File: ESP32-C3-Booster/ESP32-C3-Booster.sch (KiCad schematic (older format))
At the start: 0 parts

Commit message: Almost done with ESP32-C3-Booster.
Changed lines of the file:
@@
 F0 "ESP32-C3 MCU" 60
 F1 "ESP32-C3-MCU.sch" 60
+F2 "GPIO0/A1/CurrentSense" I L 5100 3150 60
+F3 "GPIO1/A2/TermpSense" I R 7250 2250 60
+F4 "GPIO2/Fan" O R 7250 2000 60
+F5 "CAN_TX" O L 5100 1700 60
+F6 "CAN_RX" I L 5100 1900 60
 $EndSheet
 $Sheet
@@
 F4 "BRAKE" I L 5000 4350 60
 F5 "PowerIn" I L 5000 4500 60
-F6 "A" O L 5000 4650 60
-F7 "B" O L 5000 4800 60
+F6 "A" O R 7150 4550 60
+F7 "B" O R 7150 4800 60
 F8 "Sense_Pos" O L 5000 5050 60
 F9 "Sense_Neg" O L 5000 5200 60
@@
 F2 "FAN_POWER" I L 7950 1800 60
 F3 "FAN_CONTROL" I L 7950 2000 60
-F4 "TEMP_SENSE" O L 7950 2200 60
+F4 "TEMP_SENSE" O L 7950 2250 60
 $EndSheet
+Wire Wire Line
+	3500 1700 5100 1700
+Wire Wire Line
+	3500 1900 5100 1900
+$Comp
+L +3.3V #PWR?
+U 1 1 630B61AD
+P 3750 4100
+F 0 "#PWR?" H 3750 3950 50  0001 C CNN
+F 1 "+3.3V" H 3750 4240 50  0000 C CNN
+F 2 "" H 3750 4100 50  0001 C CNN
+F 3 "" H 3750 4100 50  0001 C CNN
+	1    3750 4100
+	1    0    0    -1
+$EndComp
+Wire Wire Line
+	3750 4100 3750 4150
+Wire Wire Line
+	3750 4150 3500 4150
+$Comp
+L +12V #PWR?
+U 1 1 630B6295
+P 3800 4600
+F 0 "#PWR?" H 3800 4450 50  0001 C CNN
+F 1 "+12V" H 3800 4740 50  0000 C CNN
+F 2 "" H 3800 4600 50  0001 C CNN
+F 3 "" H 3800 4600 50  0001 C CNN
+	1    3800 4600
+	1    0    0    -1
+$EndComp
+Wire Wire Line
+	3800 4600 3500 4600
+$Comp
+L +12V #PWR?
+U 1 1 630B6906
+P 7700 1800
+F 0 "#PWR?" H 7700 1650 50  0001 C CNN
+F 1 "+12V" H 7700 1940 50  0000 C CNN
+F 2 "" H 7700 1800 50  0001 C CNN
+F 3 "" H 7700 1800 50  0001 C CNN
+	1    7700 1800
+	1    0    0    -1
+$EndComp
+Wire Wire Line
+	7950 1800 7700 1800
+Wire Wire Line
+	7950 2000 7250 2000
+Wire Wire Line
+	7950 2250 7250 2250
 $EndSCHEMATC

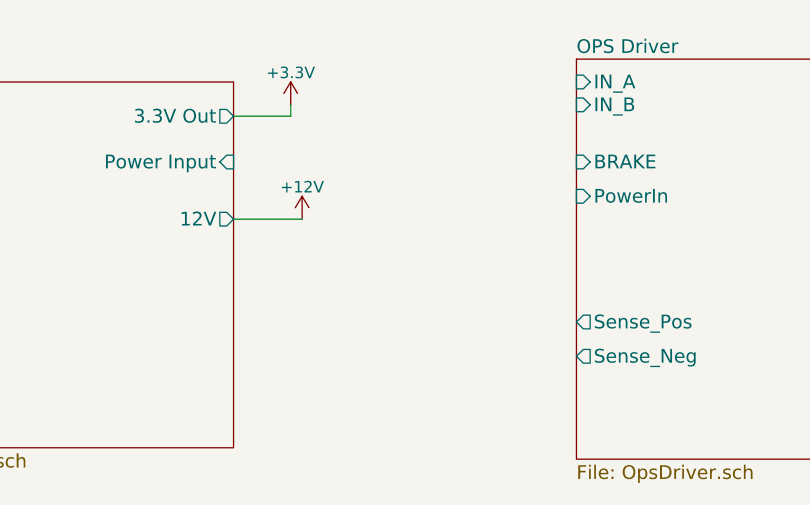
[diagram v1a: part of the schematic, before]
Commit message: Replace D_Shockley with D_Schottky.
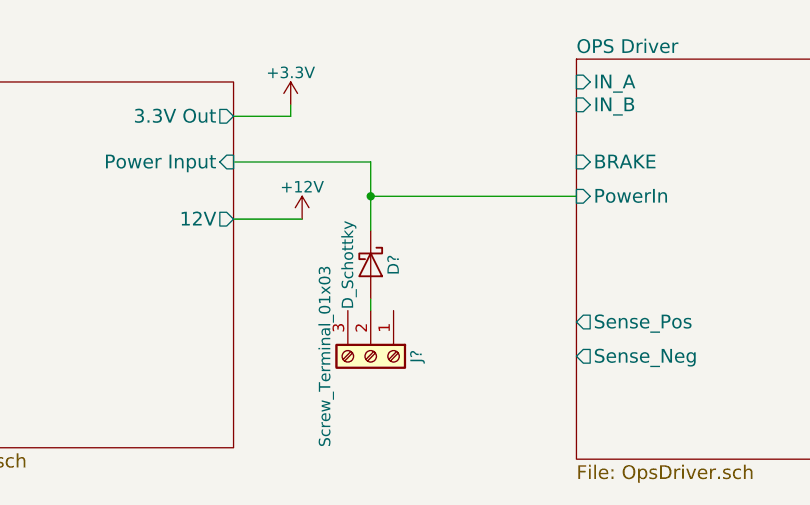
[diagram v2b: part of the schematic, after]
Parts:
- added D?: D_Schottky, symbol D_Schottky
- added J?: Screw_Terminal_01x03, symbol Screw_Terminal_01x03
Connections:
- net OPS Driver/PowerIn: now also D?.1 (K)
- new net: D?.2 (A), J?.2 (Pin_2)
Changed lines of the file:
@@
 Wire Wire Line
 	7950 2250 7250 2250
+$Comp
+L Screw_Terminal_01x03 J?
+U 1 1 630B79E1
+P 4100 5200
+F 0 "J?" H 4100 5400 50  0000 C CNN
+F 1 "Screw_Terminal_01x03" H 4100 5000 50  0000 C CNN
+F 2 "" H 4100 5200 50  0001 C CNN
+F 3 "" H 4100 5200 50  0001 C CNN
+	1    4100 5200
+	0    1    1    0
+$EndComp
+$Comp
+L D_Schottky D?
+U 1 1 630B7F8A
+P 4100 4800
+F 0 "D?" H 4100 4900 50  0000 C CNN
+F 1 "D_Schottky" H 4100 4700 50  0000 C CNN
+F 2 "" H 4100 4800 50  0001 C CNN
+F 3 "" H 4100 4800 50  0001 C CNN
+	1    4100 4800
+	0    1    1    0
+$EndComp
+Wire Wire Line
+	4100 5000 4100 4950
+Wire Wire Line
+	4100 4350 4100 4650
+Wire Wire Line
+	4100 4500 5000 4500
+Wire Wire Line
+	3500 4350 4100 4350
+Connection ~ 4100 4500
 $EndSCHEMATC

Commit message: Completed first pass ESP32-C3-Booster.
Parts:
- added C101: 10 nf, Capacitors_SMD:C_1206, symbol C_Small
- added D102: OPS ActB, LEDs:LED_0603, symbol LED
- added D103: OPS ActA, LEDs:LED_0603, symbol LED
- added F101, F102: 5A, MF-R500:MFR500, symbol Fuse_Small
- added J102: Output to tracks, Connectors_Terminal_Blocks:TerminalBlock_Pheonix_PT-3.5mm_2pol, symbol Screw_Terminal_01x02
- added R101, R103: 3K, Resistors_SMD:R_0603, symbol R
- added R102: 2.4, Resistors_SMD:R_1206, symbol R
- added U101: INA180B, TO_SOT_Packages_SMD:SOT-23-5, symbol INA180B
- D101: renamed from D?; value D_Schottky -> RB080LAM-30TR; footprint (none) -> RB080LAM-30TR:PMDTM; Mouser Part Number (none) -> 755-RB080LAM-30TR
- J101: renamed from J?; value Screw_Terminal_01x03 -> - Power + In -; footprint (none) -> Connectors_Terminal_Blocks:TerminalBlock_Pheonix_PT-3.5mm_3pol; Mouser Part Number (none) -> 651-544225
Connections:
- net +3V3: now also U101.5 (VS)
- net ESP32-C3 MCU/GPIO0/A1/CurrentSense: now also U101.4 (OUT)
- net OPS Driver/A: now also C101.1, F101.1, R103.1
- net OPS Driver/B: now also F102.1, R101.1, R102.2
- net OPS Driver/Sense_Neg: now also U101.3 (IN-)
- net OPS Driver/Sense_Pos: now also U101.1 (IN+)
- net GND: now reaches J101.1 (Pin_1)
- net GND: now also J101.3 (Pin_3), D102.1 (K), D103.1 (K), U101.2 (GND)
- new net: C101.2, R102.1
- new net: F101.2, J102.1 (Pin_1)
- new net: F102.2, J102.2 (Pin_2)
- new net: D102.2 (A), R101.2
- new net: D103.2 (A), R103.2
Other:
- moved on the sheet: J101

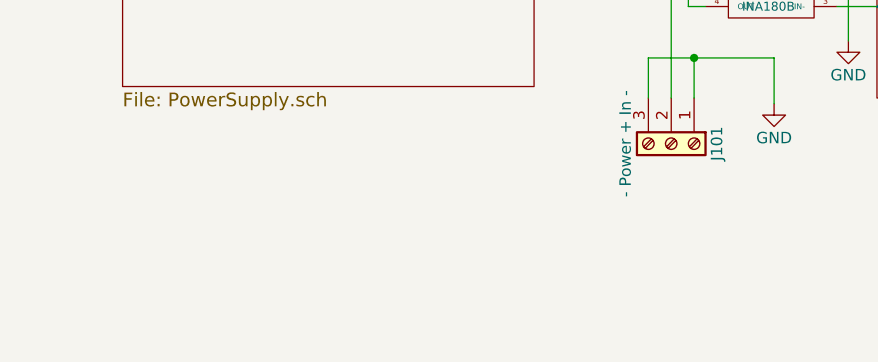
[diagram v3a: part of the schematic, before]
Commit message: Finalize ESP32-C3-Booster: mounting holes, Fids, copyright and symbols/logos, silk cleanup.
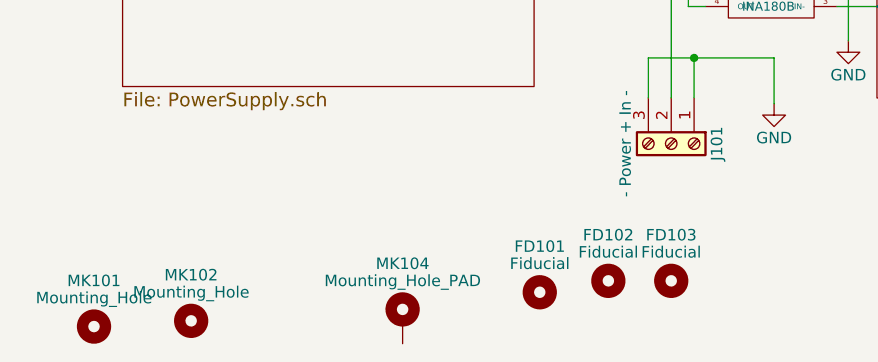
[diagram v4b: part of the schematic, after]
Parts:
- added FD101, FD102, FD103: Fiducial, Fiducials:Fiducial_classic_Small_SilkscreenTop_Type1, symbol Mounting_Hole
- added MK101, MK102: Mounting_Hole, Mounting_Holes:MountingHole_3.5mm, symbol Mounting_Hole
- added MK104: Mounting_Hole_PAD, Mounting_Holes:MountingHole_3.5mm_Pad, symbol Mounting_Hole_PAD
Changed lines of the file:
@@
 LIBS:MCP9700T-E_LT
 LIBS:ina180b
+LIBS:mechanical
 LIBS:ESP32-C3-Booster-cache
 EELAYER 25 0
@@
 	4200 5650 4200 5475
 Connection ~ 4200 5475
+$Comp
+L Mounting_Hole MK101
+U 1 1 630CC312
+P 1575 6650
+F 0 "MK101" H 1575 6850 50  0000 C CNN
+F 1 "Mounting_Hole" H 1575 6775 50  0000 C CNN
+F 2 "Mounting_Holes:MountingHole_3.5mm" H 1575 6650 50  0001 C CNN
+F 3 "" H 1575 6650 50  0001 C CNN
+	1    1575 6650
+	1    0    0    -1
+$EndComp
+$Comp
+L Mounting_Hole MK102
+U 1 1 630CC3D3
+P 2000 6625
+F 0 "MK102" H 2000 6825 50  0000 C CNN
+F 1 "Mounting_Hole" H 2000 6750 50  0000 C CNN
+F 2 "Mounting_Holes:MountingHole_3.5mm" H 2000 6625 50  0001 C CNN
+F 3 "" H 2000 6625 50  0001 C CNN
+	1    2000 6625
+	1    0    0    -1
+$EndComp
+$Comp
+L Mounting_Hole_PAD MK104
+U 1 1 630CC557
+P 2925 6625
+F 0 "MK104" H 2925 6875 50  0000 C CNN
+F 1 "Mounting_Hole_PAD" H 2925 6800 50  0000 C CNN
+F 2 "Mounting_Holes:MountingHole_3.5mm_Pad" H 2925 6625 50  0001 C CNN
+F 3 "" H 2925 6625 50  0001 C CNN
+	1    2925 6625
+	1    0    0    -1
+$EndComp
+$Comp
+L Mounting_Hole FD101
+U 1 1 630CC61E
+P 3525 6500
+F 0 "FD101" H 3525 6700 50  0000 C CNN
+F 1 "Fiducial" H 3525 6625 50  0000 C CNN
+F 2 "Fiducials:Fiducial_classic_Small_SilkscreenTop_Type1" H 3525 6500 50  0001 C CNN
+F 3 "" H 3525 6500 50  0001 C CNN
+	1    3525 6500
+	1    0    0    -1
+$EndComp
+$Comp
+L Mounting_Hole FD102
+U 1 1 630CD5D2
+P 3825 6450
+F 0 "FD102" H 3825 6650 50  0000 C CNN
+F 1 "Fiducial" H 3825 6575 50  0000 C CNN
+F 2 "Fiducials:Fiducial_classic_Small_SilkscreenTop_Type1" H 3825 6450 50  0001 C CNN
+F 3 "" H 3825 6450 50  0001 C CNN
+	1    3825 6450
+	1    0    0    -1
+$EndComp
+$Comp
+L Mounting_Hole FD103
+U 1 1 630CD6BE
+P 4100 6450
+F 0 "FD103" H 4100 6650 50  0000 C CNN
+F 1 "Fiducial" H 4100 6575 50  0000 C CNN
+F 2 "Fiducials:Fiducial_classic_Small_SilkscreenTop_Type1" H 4100 6450 50  0001 C CNN
+F 3 "" H 4100 6450 50  0001 C CNN
+	1    4100 6450
+	1    0    0    -1
+$EndComp
 $EndSCHEMATC

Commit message: Add README, Schematic, Board Rendering, and BOM for ESP32-C3-Booster.
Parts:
- U101: Mouser Part Number (none) -> 595-INA180B3IDBVR
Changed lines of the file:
@@
 F 2 "TO_SOT_Packages_SMD:SOT-23-5" H 4550 5150 60  0001 C CNN
 F 3 "" H 4550 5150 60  0001 C CNN
+F 4 "595-INA180B3IDBVR" H 4550 5150 60  0001 C CNN "Mouser Part Number"
 	1    4550 5150
 	-1   0    0    -1
